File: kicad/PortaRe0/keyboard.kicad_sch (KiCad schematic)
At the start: 0 parts

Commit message: session08: RP2040 keyboardシート作業中（RP2040本体・QSPI Flash・クリスタル・GPIO完了）
- RP2040本体配置・電源デカップリング完了
- VREG_IN/VOUT/DVDD接続完了
- クリスタル（Crystal_GND23 / 12MHz / 15pF×2）接続完了
- QSPI Flash（W25Q32）接続完了（/CS 10kΩプルアップ・BOOTSEL 1kΩ引き出し）
- RUN 10kΩプルアップ完了
- SWD/SWCLK Global Label引き出し完了
- USB_DP/USB_DM 27Ω直列抵抗・Global Label完了
- GPIO Global Label完了（I2C/I2S/LED/スティック/COL/ROW 全17+13本）
- 次：キースイッチ＆ダイオードマトリクス

Co-Authored-By: Claude Sonnet 4.6 <noreply@anthropic.com>
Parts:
- added C49, C50, C51, C54, C55, C56, C57, C61, C62, C63, C64, C69: 100nF, symbol Device:C_Small
- added C60: 1μF, symbol Device:C_Small
- added C65, C68: 15pF, symbol Device:C_Small
- added R26, R29: 10kΩ, symbol Device:R_Small
- added R27, R28: 27Ω, symbol Device:R_Small
- added R30: 1kΩ, symbol Device:R_Small
- added U6: RP2040, PortaRe0:LQFN-56_L7.0-W7.0-P0.4-EP, symbol PortaRe0:RP2040
- added U7: W25Q32JVSSIQ, PortaRe0:SOIC-8_L5.3-W5.3-P1.27-LS8.0-BL, symbol PortaRe0:W25Q32JVSSIQ
- added Y2: 12Mhz, Crystal:Crystal_SMD_3225-4Pin_3.2x2.5mm, symbol Device:Crystal_GND23_Small
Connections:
- new net: R27.2, U6.47 (USB_DP)
- new net: C65.1, U6.20 (XIN), Y2.1
- new net: Y2.2 (G), Y2.3 (G)
- new net: C68.1, U6.21 (XOUT), Y2.4
- new net: R28.2, U6.46 (USB_DM)
- new net: C60.2, C63.2, C64.2, U6.23 (DVDD), U6.45 (VREG_VOUT), U6.50 (DVDD)
- new net: R26.1, U6.26 (RUN)
- new net +3V3: C49.2, C50.2, C51.2, C54.2, C55.2, C56.2, C57.2, C61.2, C62.2, C69.1, R26.2, R29.2, U6.1 (IOVDD), U6.10 (IOVDD), U6.22 (IOVDD), U6.33 (IOVDD), U6.42 (IOVDD), U6.43 (ADC_AVDD), U6.44 (VREG_IN), U6.48 (USB_VDD), U6.49 (IOVDD), U7.8 (VCC)
- new net BOOTSEL: R30.1
- new net BQ_INT: U6.30 (GPIO19)
- new net GNDPWR: C49.1, C50.1, C51.1, C54.1, C55.1, C56.1, C57.1, C60.1, C61.1, C62.1, C63.1, C64.1, C65.2, C68.2, C69.2, U7.4 (GND)
- new net I2C_SCL: U6.28 (GPIO17)
- new net I2C_SDA: U6.29 (GPIO18)
- new net I2S_BCLK: U6.32 (GPIO21)
- new net I2S_LRCLK: U6.34 (GPIO22)
- new net I2S_SDIN: U6.35 (GPIO23)
- new net LED_ACT: U6.38 (GPIO26_ADC0)
- new net LED_CHG: U6.36 (GPIO24)
- new net LED_FULL: U6.37 (GPIO25)
- new net QSPI_SCLK: U6.52 (QSPI_SCLK), U7.6 (CLK)
- new net QSPI_SD0: U6.53 (QSPI_SD0), U7.5 (DI（IO0）)
- new net QSPI_SD1: U6.55 (QSPI_SD1), U7.2 (DO（IO1）)
- new net QSPI_SD2: U6.54 (QSPI_SD2), U7.3 (IO2)
- new net QSPI_SD3: U6.51 (QSPI_SD3), U7.7 (IO3)
- new net QSPI_SS: R29.1, R30.2, U6.56 (QSPI_SS), U7.1 (~{CS})
- new net RP2040_EN: U6.31 (GPIO20)
- new net STICK_X: U6.39 (GPIO27_ADC1)
- new net STICK_Y: U6.40 (GPIO28_ADC2)
- new net SWCLK: U6.24 (SWCLK)
- new net SWDIO: U6.25 (SWD)
- new net USB_DM: R28.1
- new net USB_DP: R27.1

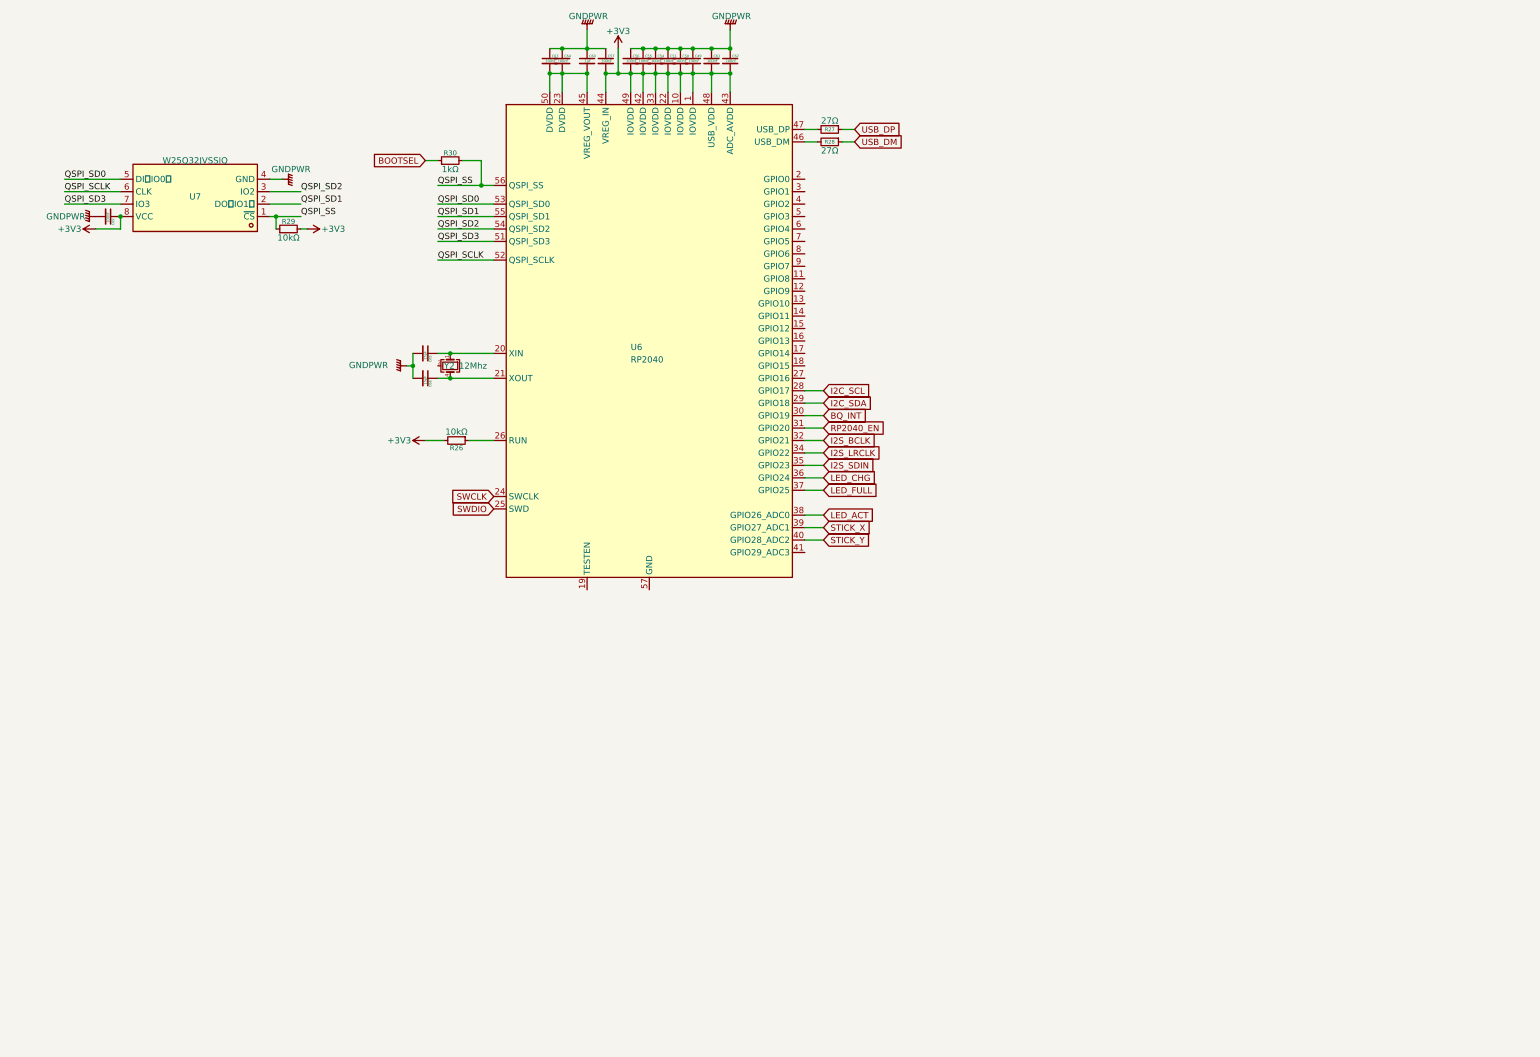
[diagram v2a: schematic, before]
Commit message: Complete keyboard sheet: analog stick, LED circuits
- アナログスティック回路: Molex 5034800440 FPCコネクタ
  Pin1=GND / Pin2=GP27(X) / Pin3=+3V3 / Pin4=GP28(Y)
  デカップリング 100nF
- LED回路 x3:
  +3V3 - 330Ω - LED_CHG(GP24) / LED_FULL(GP25) / LED_ACT(GP26)
  アクティブLow

keyboardシート完成

Co-Authored-By: Claude Sonnet 4.6 <noreply@anthropic.com>
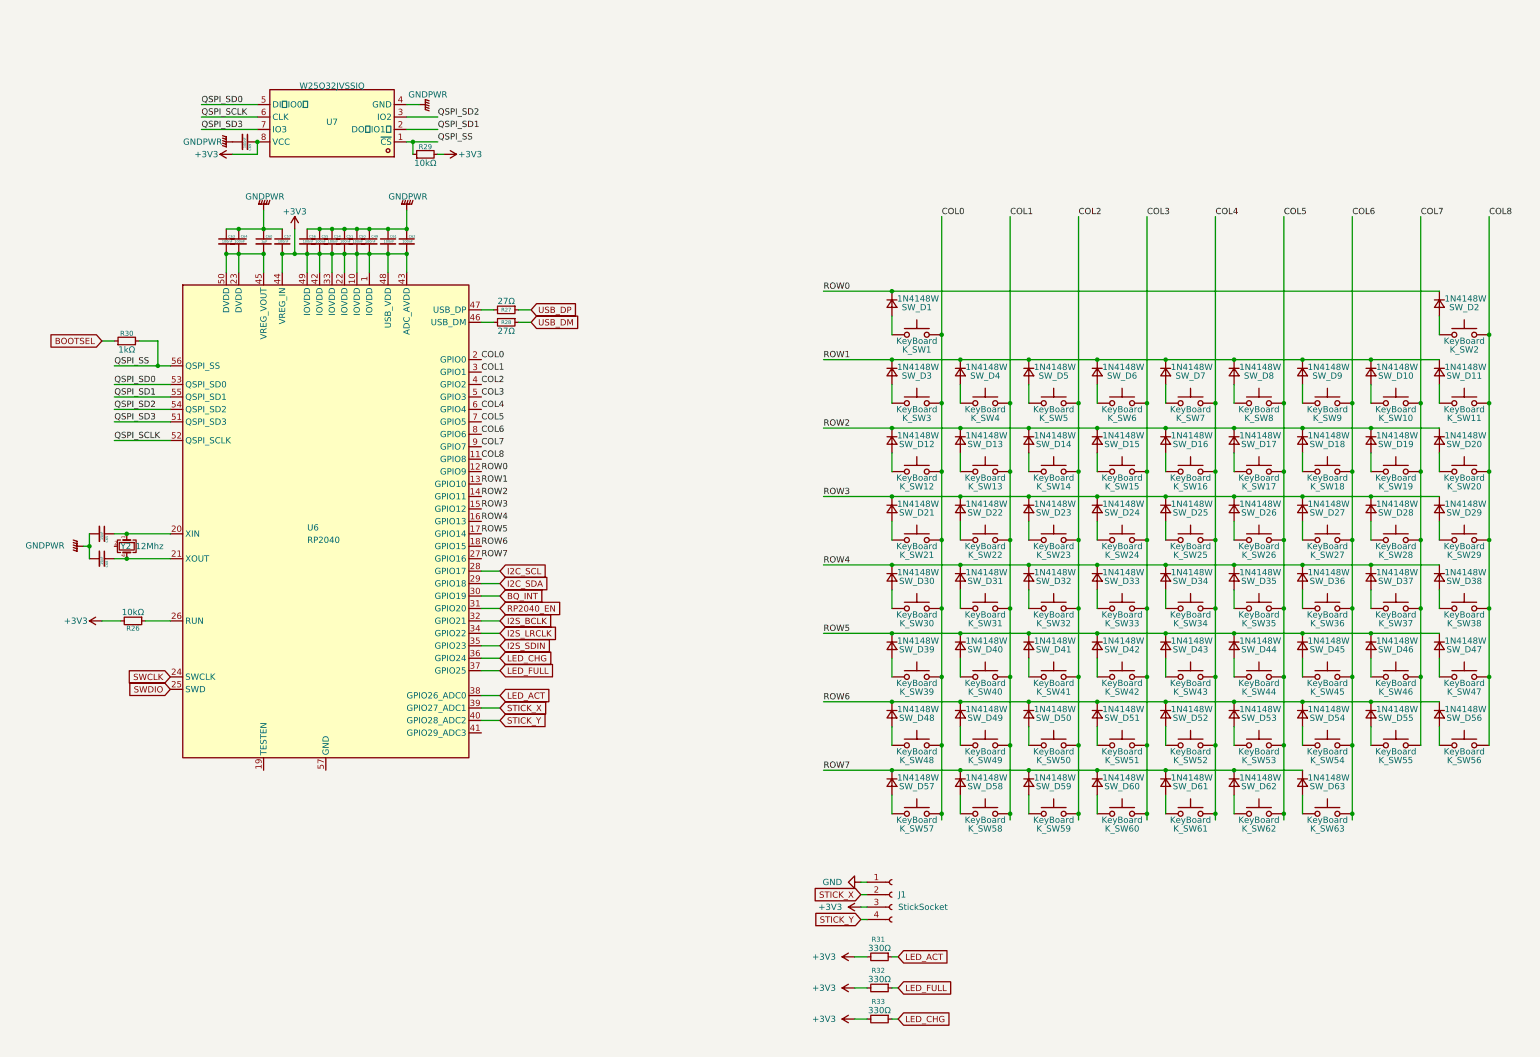
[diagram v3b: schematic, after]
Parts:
- added J1: StickSocket, PortaRe0:FPC-SMD_5034800400, symbol Connector:Conn_01x04_Socket
- added K_SW1, K_SW10, K_SW11, K_SW12, K_SW13, K_SW14, K_SW15, K_SW16, K_SW17, K_SW18, K_SW19, K_SW2, K_SW20, K_SW21, K_SW22, K_SW23, K_SW24, K_SW25, K_SW26, K_SW27, K_SW28, K_SW29, K_SW3, K_SW30, K_SW31, K_SW32, K_SW33, K_SW34, K_SW35, K_SW36, K_SW37, K_SW38, K_SW39, K_SW4, K_SW40, K_SW41, K_SW42, K_SW43, K_SW44, K_SW45, K_SW46, K_SW47, K_SW48, K_SW49, K_SW5, K_SW50, K_SW51, K_SW52, K_SW53, K_SW54, K_SW55, K_SW56, K_SW57, K_SW58, K_SW59, K_SW6, K_SW60, K_SW61, K_SW62, K_SW63, K_SW7, K_SW8, K_SW9: KeyBoard, symbol Switch:SW_Push
- added R31, R32, R33: 330Ω, symbol Device:R_Small
- added SW_D1, SW_D10, SW_D11, SW_D12, SW_D13, SW_D14, SW_D15, SW_D16, SW_D17, SW_D18, SW_D19, SW_D2, SW_D20, SW_D21, SW_D22, SW_D23, SW_D24, SW_D25, SW_D26, SW_D27, SW_D28, SW_D29, SW_D3, SW_D30, SW_D31, SW_D32, SW_D33, SW_D34, SW_D35, SW_D36, SW_D37, SW_D38, SW_D39, SW_D4, SW_D40, SW_D41, SW_D42, SW_D43, SW_D44, SW_D45, SW_D46, SW_D47, SW_D48, SW_D49, SW_D5, SW_D50, SW_D51, SW_D52, SW_D53, SW_D54, SW_D55, SW_D56, SW_D57, SW_D58, SW_D59, SW_D6, SW_D60, SW_D61, SW_D62, SW_D63, SW_D7, SW_D8, SW_D9: 1N4148W, symbol Device:D_Small
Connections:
- net +3V3: now also J1.3 (Pin_3), R31.2, R32.2, R33.2
- net LED_ACT: now also R31.1
- net LED_CHG: now also R33.1
- net LED_FULL: now also R32.1
- net STICK_X: now also J1.2 (Pin_2)
- net STICK_Y: now also J1.4 (Pin_4)
- net COL8: now reaches U6.11 (GPIO8)
- net COL8: now also K_SW11.2, K_SW2.2, K_SW20.2, K_SW29.2, K_SW38.2, K_SW47.2, K_SW56.2
- net ROW0: now reaches U6.12 (GPIO9)
- net ROW0: now also SW_D1.1 (K), SW_D2.1 (K)
- net ROW1: now reaches U6.13 (GPIO10)
- net ROW1: now also SW_D10.1 (K), SW_D11.1 (K), SW_D3.1 (K), SW_D4.1 (K), SW_D5.1 (K), SW_D6.1 (K), SW_D7.1 (K), SW_D8.1 (K), SW_D9.1 (K)
- net ROW2: now reaches U6.14 (GPIO11)
- net ROW2: now also SW_D12.1 (K), SW_D13.1 (K), SW_D14.1 (K), SW_D15.1 (K), SW_D16.1 (K), SW_D17.1 (K), SW_D18.1 (K), SW_D19.1 (K), SW_D20.1 (K)
- net ROW3: now reaches U6.15 (GPIO12)
- net ROW3: now also SW_D21.1 (K), SW_D22.1 (K), SW_D23.1 (K), SW_D24.1 (K), SW_D25.1 (K), SW_D26.1 (K), SW_D27.1 (K), SW_D28.1 (K), SW_D29.1 (K)
- net ROW4: now reaches U6.16 (GPIO13)
- net ROW4: now also SW_D30.1 (K), SW_D31.1 (K), SW_D32.1 (K), SW_D33.1 (K), SW_D34.1 (K), SW_D35.1 (K), SW_D36.1 (K), SW_D37.1 (K), SW_D38.1 (K)
- net ROW5: now reaches U6.17 (GPIO14)
- net ROW5: now also SW_D39.1 (K), SW_D40.1 (K), SW_D41.1 (K), SW_D42.1 (K), SW_D43.1 (K), SW_D44.1 (K), SW_D45.1 (K), SW_D46.1 (K), SW_D47.1 (K)
- net ROW6: now reaches U6.18 (GPIO15)
- net ROW6: now also SW_D48.1 (K), SW_D49.1 (K), SW_D50.1 (K), SW_D51.1 (K), SW_D52.1 (K), SW_D53.1 (K), SW_D54.1 (K), SW_D55.1 (K), SW_D56.1 (K)
- net COL0: now reaches U6.2 (GPIO0)
- net COL0: now also K_SW1.2, K_SW12.2, K_SW21.2, K_SW3.2, K_SW30.2, K_SW39.2, K_SW48.2, K_SW57.2
- net ROW7: now reaches U6.27 (GPIO16)
- net ROW7: now also SW_D57.1 (K), SW_D58.1 (K), SW_D59.1 (K), SW_D60.1 (K), SW_D61.1 (K), SW_D62.1 (K), SW_D63.1 (K)
- net COL1: now reaches U6.3 (GPIO1)
- net COL1: now also K_SW13.2, K_SW22.2, K_SW31.2, K_SW4.2, K_SW40.2, K_SW49.2, K_SW58.2
- net COL2: now reaches U6.4 (GPIO2)
- net COL2: now also K_SW14.2, K_SW23.2, K_SW32.2, K_SW41.2, K_SW5.2, K_SW50.2, K_SW59.2
- net COL3: now reaches U6.5 (GPIO3)
- net COL3: now also K_SW15.2, K_SW24.2, K_SW33.2, K_SW42.2, K_SW51.2, K_SW6.2, K_SW60.2
- net COL4: now reaches U6.6 (GPIO4)
- net COL4: now also K_SW16.2, K_SW25.2, K_SW34.2, K_SW43.2, K_SW52.2, K_SW61.2, K_SW7.2
- net COL5: now reaches U6.7 (GPIO5)
- net COL5: now also K_SW17.2, K_SW26.2, K_SW35.2, K_SW44.2, K_SW53.2, K_SW62.2, K_SW8.2
- net COL6: now reaches U6.8 (GPIO6)
- net COL6: now also K_SW18.2, K_SW27.2, K_SW36.2, K_SW45.2, K_SW54.2, K_SW63.2, K_SW9.2
- net COL7: now reaches U6.9 (GPIO7)
- net COL7: now also K_SW10.2, K_SW19.2, K_SW28.2, K_SW37.2, K_SW46.2, K_SW55.2
- new net: K_SW39.1, SW_D39.2 (A)
- new net: K_SW7.1, SW_D7.2 (A)
- new net: K_SW58.1, SW_D58.2 (A)
- new net: K_SW12.1, SW_D12.2 (A)
- new net: K_SW22.1, SW_D22.2 (A)
- new net: K_SW19.1, SW_D19.2 (A)
- new net: K_SW15.1, SW_D15.2 (A)
- new net: K_SW4.1, SW_D4.2 (A)
- new net: K_SW17.1, SW_D17.2 (A)
- new net: K_SW47.1, SW_D47.2 (A)
- new net: K_SW20.1, SW_D20.2 (A)
- new net: K_SW9.1, SW_D9.2 (A)
- new net: K_SW24.1, SW_D24.2 (A)
- new net: K_SW38.1, SW_D38.2 (A)
- new net: K_SW21.1, SW_D21.2 (A)
- new net: K_SW1.1, SW_D1.2 (A)
- new net: K_SW42.1, SW_D42.2 (A)
- new net: K_SW8.1, SW_D8.2 (A)
- new net: K_SW45.1, SW_D45.2 (A)
- new net: K_SW41.1, SW_D41.2 (A)
- new net: K_SW48.1, SW_D48.2 (A)
- new net: K_SW35.1, SW_D35.2 (A)
- new net: K_SW49.1, SW_D49.2 (A)
- new net: K_SW54.1, SW_D54.2 (A)
- new net: K_SW14.1, SW_D14.2 (A)
- new net: K_SW37.1, SW_D37.2 (A)
- new net: K_SW18.1, SW_D18.2 (A)
- new net: K_SW53.1, SW_D53.2 (A)
- new net: K_SW25.1, SW_D25.2 (A)
- new net: K_SW23.1, SW_D23.2 (A)
- new net: K_SW52.1, SW_D52.2 (A)
- new net: K_SW44.1, SW_D44.2 (A)
- new net: K_SW28.1, SW_D28.2 (A)
- new net: K_SW31.1, SW_D31.2 (A)
- new net: K_SW10.1, SW_D10.2 (A)
- new net: K_SW50.1, SW_D50.2 (A)
- new net: K_SW34.1, SW_D34.2 (A)
- new net: K_SW33.1, SW_D33.2 (A)
- new net: K_SW61.1, SW_D61.2 (A)
- new net: K_SW56.1, SW_D56.2 (A)
- new net: K_SW36.1, SW_D36.2 (A)
- new net: K_SW51.1, SW_D51.2 (A)
- new net: K_SW40.1, SW_D40.2 (A)
- new net: K_SW29.1, SW_D29.2 (A)
- new net: K_SW30.1, SW_D30.2 (A)
- new net: K_SW16.1, SW_D16.2 (A)
- new net: K_SW62.1, SW_D62.2 (A)
- new net: K_SW57.1, SW_D57.2 (A)
- new net: K_SW43.1, SW_D43.2 (A)
- new net: K_SW55.1, SW_D55.2 (A)
- new net: K_SW59.1, SW_D59.2 (A)
- new net: K_SW3.1, SW_D3.2 (A)
- new net: K_SW11.1, SW_D11.2 (A)
- new net: K_SW27.1, SW_D27.2 (A)
- new net: K_SW26.1, SW_D26.2 (A)
- new net: K_SW6.1, SW_D6.2 (A)
- new net: K_SW60.1, SW_D60.2 (A)
- new net: K_SW46.1, SW_D46.2 (A)
- new net: K_SW63.1, SW_D63.2 (A)
- new net: K_SW2.1, SW_D2.2 (A)
- new net: K_SW13.1, SW_D13.2 (A)
- new net: K_SW32.1, SW_D32.2 (A)
- new net: K_SW5.1, SW_D5.2 (A)
- new net GND: J1.1 (Pin_1)
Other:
- moved on the sheet: C49, C50, C51, C54, C55, C56, C57, C60, C61, C62, C63, C64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

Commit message: Fix dangling wires in keyboard sheet
端の余り配線を修正

Co-Authored-By: Claude Sonnet 4.6 <noreply@anthropic.com>
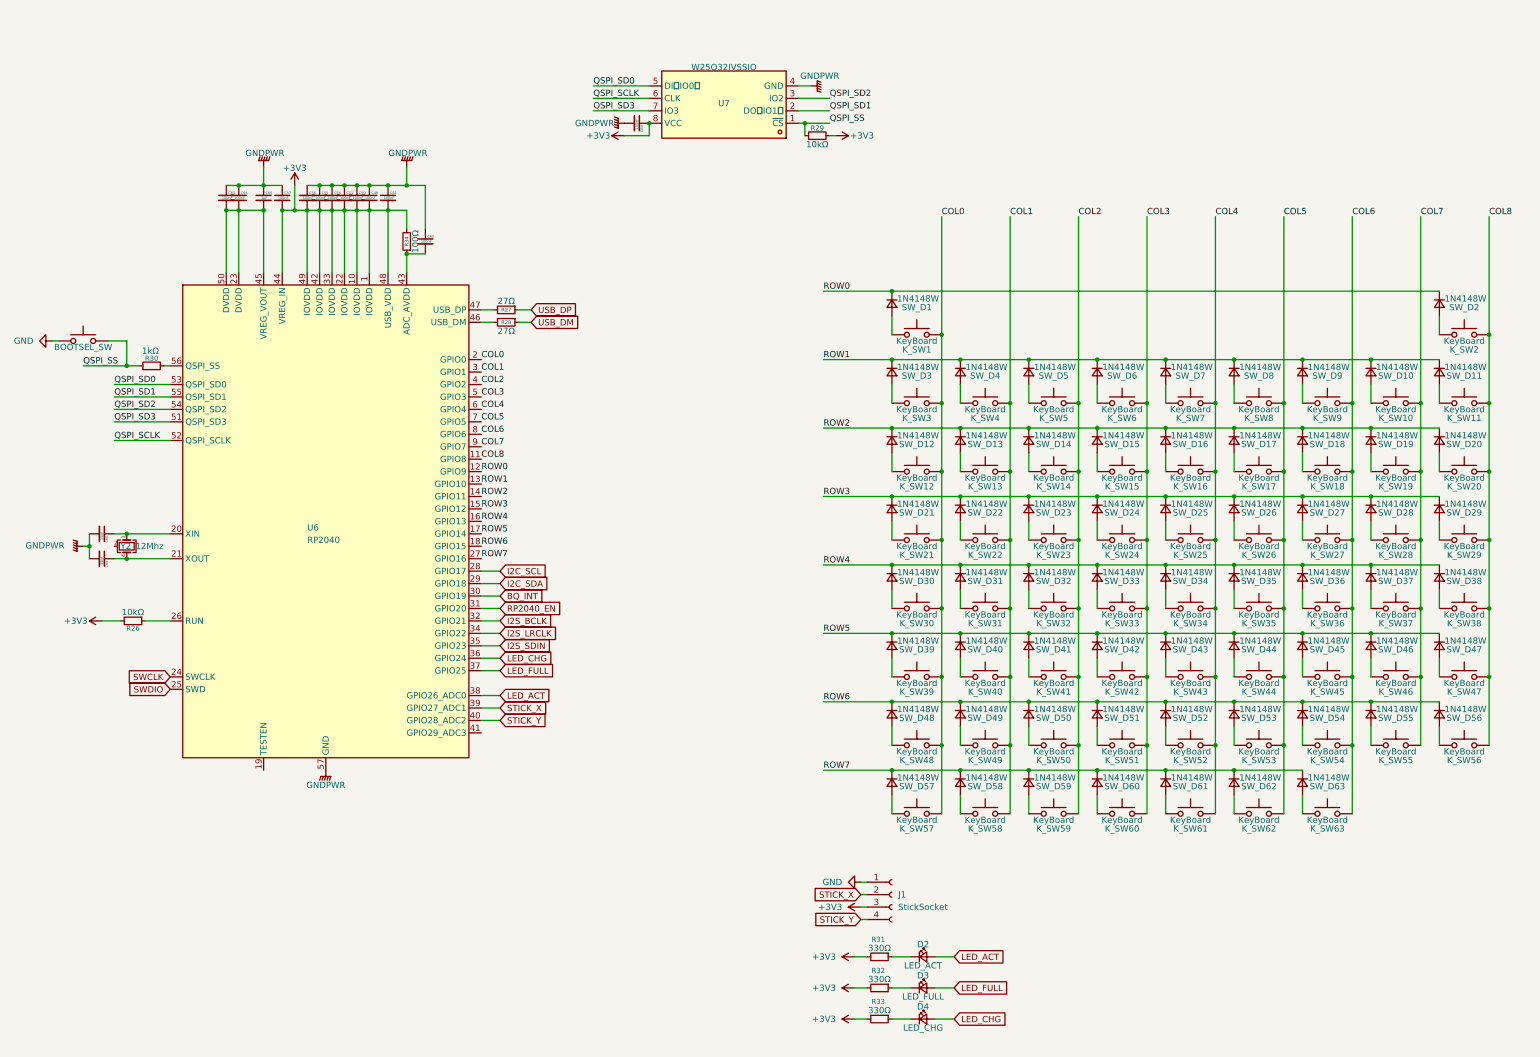
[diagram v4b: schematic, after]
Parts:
- added D2: LED_ACT, symbol Device:LED_Small
- added D3: LED_FULL, symbol Device:LED_Small
- added D4: LED_CHG, symbol Device:LED_Small
- added K_SW64: BOOTSEL_SW, symbol Switch:SW_Push
- added R34: 100Ω, symbol Device:R_Small
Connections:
- net BOOTSEL is gone; now on net QSPI_SS: R30.1
- net +3V3: now also R34.2; no longer C62.2, U6.43 (ADC_AVDD)
- net GND: now also K_SW64.1
- net GNDPWR: now also U6.57 (GND)
- net LED_ACT: now also D2.2 (A); no longer R31.1
- net LED_CHG: now also D4.2 (A); no longer R33.1
- net LED_FULL: now also D3.2 (A); no longer R32.1
- net QSPI_SS: now also K_SW64.2; no longer R30.2, U6.56 (QSPI_SS)
- new net: D3.1 (K), R32.1
- new net: C62.2, R34.1, U6.43 (ADC_AVDD)
- new net: D4.1 (K), R33.1
- new net: D2.1 (K), R31.1
- new net: R30.2, U6.56 (QSPI_SS)
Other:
- moved on the sheet: C49, C50, C51, C54, C55, C56, C57, C60, C61, C62, C63, C64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
